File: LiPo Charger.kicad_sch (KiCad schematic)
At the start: 16 parts, among them J1 Battery_conn_in, J2 Battery_conn_out, J3 Charger_conn, U1 BQ24090DGQ, U2 XB8089D

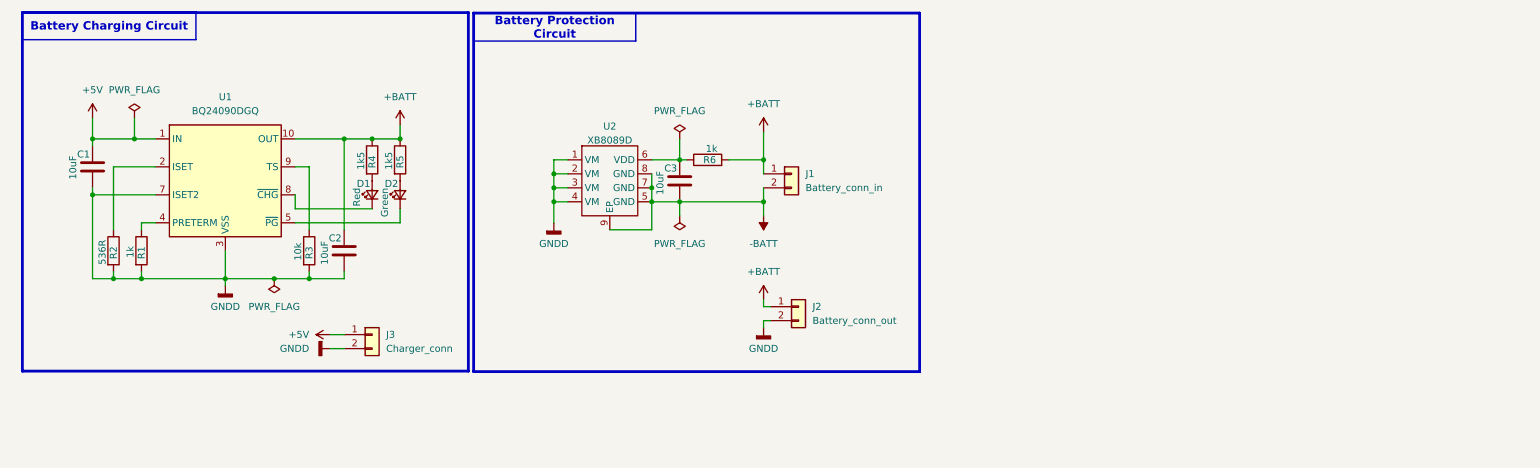
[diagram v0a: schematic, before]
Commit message: feat: battery active balancing is now added.
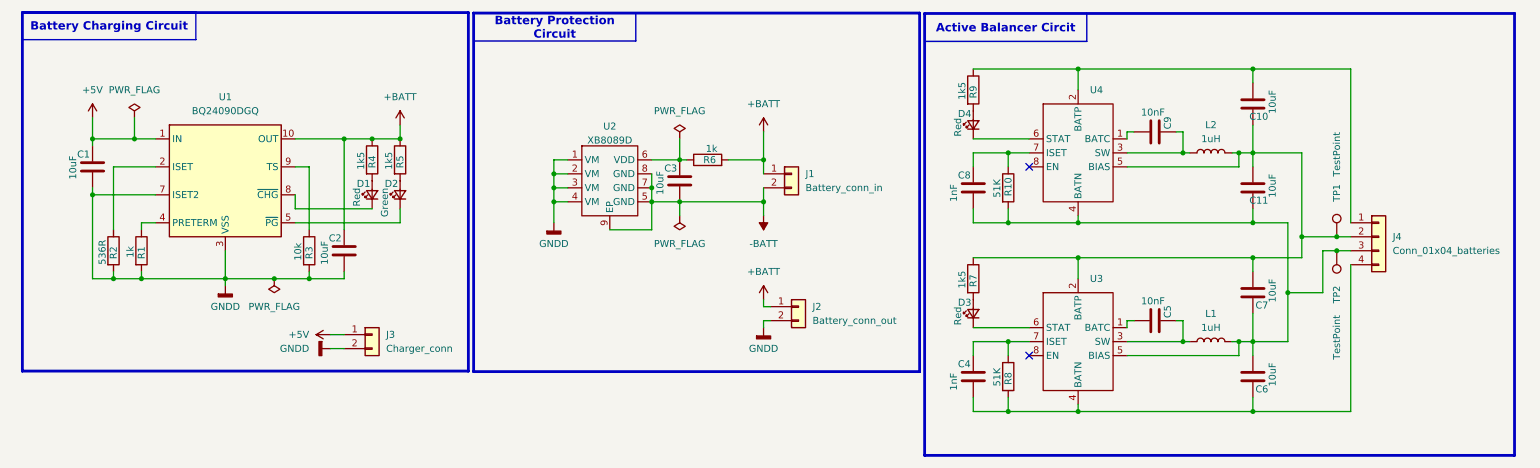
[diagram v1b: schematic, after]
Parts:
- added C10, C11, C6, C7: 10uF, Capacitor_SMD:C_0402_1005Metric_Pad0.74x0.62mm_HandSolder, symbol Device:C
- added C4, C8: 1nF, Capacitor_SMD:C_0402_1005Metric_Pad0.74x0.62mm_HandSolder, symbol Device:C
- added C5, C9: 10nF, Capacitor_SMD:C_0402_1005Metric_Pad0.74x0.62mm_HandSolder, symbol Device:C
- added D3, D4: Red, SparkFun-LED:LED_0603_1608Metric_Red, symbol SparkFun-LED:LED_Red_0603
- added J4: Conn_01x04_batteries, Connector_JST:JST_EH_B4B-EH-A_1x04_P2.50mm_Vertical, symbol Connector_Generic:Conn_01x04
- added L1, L2: 1uH, Inductor_SMD:L_Sunlord_SWPA3010S, symbol Device:L
- added R10, R8: 51K, PCM_Resistor_SMD_AKL:R_0201_0603Metric_Pad0.64x0.40mm_HandSolder, symbol Device:R
- added R7, R9: 1k5, PCM_Resistor_SMD_AKL:R_0201_0603Metric_Pad0.64x0.40mm_HandSolder, symbol Device:R
- added TP1, TP2: TestPoint, TestPoint:TestPoint_Pad_D1.5mm, symbol Connector:TestPoint
- added U3, U4: ~, Package_DFN_QFN:DFN-8-1EP_2x2mm_P0.5mm_EP0.6x1.2mm, symbol Chineness:ETA3000
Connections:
- new net: C10.1, C11.2, C7.2, J4.2 (Pin_2), L2.2, R7.1, TP1.1, U3.2 (BATP), U4.5 (BIAS)
- new net: C8.1, R10.1, U4.7 (ISET)
- new net: C11.1, C6.2, C7.1, C8.2, J4.3 (Pin_3), L1.2, R10.2, TP2.1, U3.5 (BIAS), U4.4 (BATN)
- new net: C10.2, J4.1 (Pin_1), R9.1, U4.2 (BATP)
- new net: C4.1, R8.1, U3.7 (ISET)
- new net: C4.2, C6.1, J4.4 (Pin_4), R8.2, U3.4 (BATN)
- new net: D3.2 (A), R7.2
- new net: C5.2, U3.1 (BATC)
- new net: C5.1, L1.1, U3.3 (SW)
- new net: D3.1 (K), U3.6 (STAT)
- new net: D4.2 (A), R9.2
- new net: C9.2, U4.1 (BATC)
- new net: C9.1, L2.1, U4.3 (SW)
- new net: D4.1 (K), U4.6 (STAT)
- no-connect marks 0 -> 2

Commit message: making production files for PCBA.
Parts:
- U3, U4: value ~ -> ETA3000
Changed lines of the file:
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@@
 			)
 		)
-		(property "Value" "~"
+		(property "Value" "ETA3000"
 			(at 204.47 72.39 0)
 			(effects
@@
 	)
 	(symbol
-		(lib_name "ETA3000_1")
 		(lib_id "Chineness:ETA3000")
 		(at 204.47 38.1 0)
@@
 			)
 		)
-		(property "Value" "~"
+		(property "Value" "ETA3000"
 			(at 204.47 38.1 0)
 			(effects
